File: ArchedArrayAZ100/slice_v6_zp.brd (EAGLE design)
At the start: 196.4 x 249.7 mm, 118 parts

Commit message: ArchedArray before moving board 6
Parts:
- removed F1: (no value), ZacksLib2:LITTLEFUSE_111_501
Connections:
- removed net N$284: F1.P2_1, F1.P2_2, U$1.P$2
- net N$1: now also D10.3; no longer D10.1
- net N$100: now also D43.3; no longer D43.1
- net N$101: now also D43.1; no longer D43.3
- net N$103: now also D44.3; no longer D44.1
- net N$104: now also D44.1; no longer D44.3
- net N$106: now also D40.3; no longer D40.1
- net N$107: now also D40.1; no longer D40.3
- net N$109: now also D35.3; no longer D35.1
- net N$11: now also D12.3; no longer D12.1
- net N$110: now also D35.1; no longer D35.3
- net N$113: now also D48.1; no longer D48.3
- net N$114: now also D48.3; no longer D48.1
- net N$115: now also D47.3; no longer D47.1
- net N$116: now also D47.1; no longer D47.3
- net N$119: now also D37.3; no longer D37.1
- net N$12: now also D12.1; no longer D12.3
- net N$121: now also D38.1; no longer D38.3
- net N$122: now also D34.3; no longer D34.1
- net N$123: now also D36.1; no longer D36.3
- net N$124: now also D36.3; no longer D36.1
- net N$125: now also D37.1; no longer D37.3
- net N$126: now also D38.3; no longer D38.1
- net N$127: now also D34.1; no longer D34.3
- net N$130: now also D41.3; no longer D41.1
- net N$131: now also D41.1; no longer D41.3
- net N$133: now also D33.3; no longer D33.1
- net N$135: now also D45.3; no longer D45.1
- net N$136: now also D45.1; no longer D45.3
- net N$139: now also D46.3; no longer D46.1
- net N$14: now also D8.3; no longer D8.1
- net N$140: now also D33.1; no longer D33.3
- net N$141: now also D46.1; no longer D46.3
- net N$142: now also D58.3; no longer D58.1
- net N$144: now also D55.3; no longer D55.1
- net N$145: now also D55.1; no longer D55.3
- net N$147: now also D59.3; no longer D59.1
- net N$148: now also D59.1; no longer D59.3
- net N$15: now also D8.1; no longer D8.3
- net N$150: now also D60.3; no longer D60.1
- net N$151: now also D60.1; no longer D60.3
- net N$153: now also D56.3; no longer D56.1
- net N$154: now also D56.1; no longer D56.3
- net N$156: now also D51.3; no longer D51.1
- net N$157: now also D51.1; no longer D51.3
- net N$160: now also D64.1; no longer D64.3
- net N$161: now also D64.3; no longer D64.1
- net N$162: now also D63.3; no longer D63.1
- net N$163: now also D63.1; no longer D63.3
- net N$166: now also D53.3; no longer D53.1
- net N$168: now also D54.1; no longer D54.3
- net N$169: now also D50.3; no longer D50.1
- net N$17: now also D3.1; no longer D3.3
- net N$170: now also D52.1; no longer D52.3
- net N$171: now also D52.3; no longer D52.1
- net N$172: now also D53.1; no longer D53.3
- net N$173: now also D54.3; no longer D54.1
- net N$174: now also D50.1; no longer D50.3
- net N$177: now also D57.3; no longer D57.1
- net N$178: now also D57.1; no longer D57.3
- net N$180: now also D49.3; no longer D49.1
- net N$182: now also D61.3; no longer D61.1
- net N$183: now also D61.1; no longer D61.3
- net N$186: now also D62.3; no longer D62.1
- net N$187: now also D49.1; no longer D49.3
- net N$188: now also D62.1; no longer D62.3
- net N$189: now also D74.3; no longer D74.1
- net N$191: now also D71.3; no longer D71.1
- net N$192: now also D71.1; no longer D71.3
- net N$194: now also D75.3; no longer D75.1
- net N$195: now also D75.1; no longer D75.3
- net N$197: now also D76.3; no longer D76.1
- net N$198: now also D76.1; no longer D76.3
- net N$2: now also D3.3; no longer D3.1
- net N$20: now also D16.1; no longer D16.3
- net N$200: now also D72.3; no longer D72.1
- net N$201: now also D72.1; no longer D72.3
- net N$203: now also D67.3; no longer D67.1
- net N$204: now also D67.1; no longer D67.3
- net N$207: now also D80.1; no longer D80.3
- net N$208: now also D80.3; no longer D80.1
- net N$209: now also D79.3; no longer D79.1
- net N$21: now also D16.3; no longer D16.1
- net N$210: now also D79.1; no longer D79.3
- net N$213: now also D69.3; no longer D69.1
- net N$215: now also D70.1; no longer D70.3
- net N$216: now also D66.3; no longer D66.1
- net N$217: now also D68.1; no longer D68.3
- net N$218: now also D68.3; no longer D68.1
- net N$219: now also D69.1; no longer D69.3
- net N$22: now also D15.3; no longer D15.1
- net N$220: now also D70.3; no longer D70.1
- net N$221: now also D66.1; no longer D66.3
- net N$224: now also D73.3; no longer D73.1
- net N$225: now also D73.1; no longer D73.3
- net N$227: now also D65.3; no longer D65.1
- net N$229: now also D77.3; no longer D77.1
- net N$23: now also D15.1; no longer D15.3
- net N$230: now also D77.1; no longer D77.3
- net N$233: now also D78.3; no longer D78.1
- net N$234: now also D65.1; no longer D65.3
- net N$235: now also D78.1; no longer D78.3
- net N$236: now also D90.3; no longer D90.1
- net N$238: now also D87.3; no longer D87.1
- net N$239: now also D87.1; no longer D87.3
- net N$241: now also D91.3; no longer D91.1
- net N$242: now also D91.1; no longer D91.3
- net N$244: now also D92.3; no longer D92.1
- net N$245: now also D92.1; no longer D92.3
- net N$247: now also D88.3; no longer D88.1
- net N$248: now also D88.1; no longer D88.3
- net N$25: now also D9.1; no longer D9.3
- net N$250: now also D83.3; no longer D83.1
- net N$251: now also D83.1; no longer D83.3
- net N$254: now also D96.1; no longer D96.3
- net N$255: now also D96.3; no longer D96.1
- net N$256: now also D95.3; no longer D95.1
- net N$257: now also D95.1; no longer D95.3
- net N$26: now also D4.1; no longer D4.3
- net N$260: now also D85.3; no longer D85.1
- net N$262: now also D86.1; no longer D86.3
- net N$263: now also D82.3; no longer D82.1
- net N$264: now also D84.1; no longer D84.3
- net N$265: now also D84.3; no longer D84.1
- net N$266: now also D85.1; no longer D85.3
- net N$267: now also D86.3; no longer D86.1
- net N$268: now also D82.1; no longer D82.3
- net N$27: now also D4.3; no longer D4.1
- net N$271: now also D89.3; no longer D89.1
- net N$272: now also D89.1; no longer D89.3
- net N$274: now also D81.3; no longer D81.1
- net N$276: now also D93.3; no longer D93.1
- net N$277: now also D93.1; no longer D93.3
- net N$28: now also D5.1; no longer D5.3
- net N$280: now also D94.3; no longer D94.1
- net N$281: now also D81.1; no longer D81.3
- net N$282: now also D94.1; no longer D94.3
- net N$288: now also D90.1; no longer D90.3
- net N$289: now also D42.1; no longer D42.3
- net N$290: now also D26.1; no longer D26.3
- net N$293: now also D10.1; no longer D10.3
- net N$298: now also D74.1; no longer D74.3
- net N$300: now also D58.1; no longer D58.3
- net N$31: now also D5.3; no longer D5.1
- net N$33: now also D6.1; no longer D6.3
- net N$34: now also D1.3; no longer D1.1
- net N$35: now also D2.3; no longer D2.1
- net N$36: now also D14.1; no longer D14.3
- net N$38: now also D6.3; no longer D6.1
- net N$39: now also D13.3; no longer D13.1
- net N$4: now also D7.3; no longer D7.1
- net N$40: now also D13.1; no longer D13.3
- net N$42: now also D2.1; no longer D2.3
- net N$45: now also D26.3; no longer D26.1
- net N$47: now also D14.3; no longer D14.1
- net N$49: now also D1.1; no longer D1.3
- net N$5: now also D7.1; no longer D7.3
- net N$50: now also D23.3; no longer D23.1
- net N$51: now also D23.1; no longer D23.3
- net N$53: now also D27.3; no longer D27.1
- net N$54: now also D27.1; no longer D27.3
- net N$56: now also D28.3; no longer D28.1
- net N$57: now also D28.1; no longer D28.3
- net N$59: now also D24.3; no longer D24.1
- net N$60: now also D24.1; no longer D24.3
- net N$62: now also D19.3; no longer D19.1
- net N$63: now also D19.1; no longer D19.3
- net N$66: now also D32.1; no longer D32.3
- net N$67: now also D32.3; no longer D32.1
- net N$68: now also D31.3; no longer D31.1
- net N$69: now also D31.1; no longer D31.3
- net N$7: now also D11.3; no longer D11.1
- net N$72: now also D21.3; no longer D21.1
- net N$74: now also D22.1; no longer D22.3
- net N$75: now also D18.3; no longer D18.1
- net N$76: now also D20.1; no longer D20.3
- net N$77: now also D20.3; no longer D20.1
- net N$78: now also D21.1; no longer D21.3
- net N$79: now also D22.3; no longer D22.1
- net N$8: now also D9.3; no longer D9.1
- net N$80: now also D18.1; no longer D18.3
- net N$83: now also D25.3; no longer D25.1
- net N$84: now also D25.1; no longer D25.3
- net N$86: now also D17.3; no longer D17.1
- net N$88: now also D29.3; no longer D29.1
- net N$89: now also D29.1; no longer D29.3
- net N$9: now also D11.1; no longer D11.3
- net N$92: now also D30.3; no longer D30.1
- net N$93: now also D17.1; no longer D17.3
- net N$94: now also D30.1; no longer D30.3
- net N$95: now also D42.3; no longer D42.1
- net N$97: now also D39.3; no longer D39.1
- net N$98: now also D39.1; no longer D39.3
- net VCC: now also U$1.P$2; no longer F1.P1_1, F1.P1_2
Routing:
- net GSCLK: track 81.2 -> 357.9 mm, vias 2 -> 11
- net VCC: track 1271.0 -> 1304.7 mm, vias 24 -> 22
- net N$284: track 11.3 -> 0.00 mm
- net N$126: track 30.0 -> 24.7 mm
- net N$4: track 30.6 -> 26.2 mm, vias 3 -> 1
- net N$125: track 18.3 -> 14.4 mm
- net N$22: track 32.1 -> 28.4 mm
- net N$2: track 31.1 -> 27.6 mm
- net N$110: track 28.4 -> 25.1 mm
- net N$20: track 52.2 -> 48.9 mm
- net N$139: track 23.0 -> 19.8 mm
- net N$293: track 56.3 -> 53.2 mm
- net N$114: track 24.0 -> 21.0 mm
- net N$141: track 21.1 -> 18.1 mm
- net N$100: track 24.7 -> 21.8 mm
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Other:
- board text removed: "7A Fuse"

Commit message: finished wiring Arched Array
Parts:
- moved U$1 34.0 mm to (98.0, 249.0), turned to 0 degrees
- moved D2 19.8 mm to (110.5, 208.0)
- moved D12 19.3 mm to (96.5, 208.0), turned to 90 degrees
- moved D8 19.2 mm to (82.5, 221.0), turned to 270 degrees
- moved CHIP_6 19.2 mm to (96.5, 218.5)
- moved D1 19.2 mm to (108.0, 216.0)
- moved D14 19.2 mm to (113.5, 216.0)
- moved D4 19.2 mm to (101.5, 208.0)
- moved D5 19.2 mm to (113.5, 224.0)
- moved D6 19.2 mm to (108.5, 224.0)
- moved D16 17.7 mm to (87.5, 225.5), turned to 270 degrees
- moved D13 16.7 mm to (113.5, 210.5)
- moved D10 15.6 mm to (78.5, 220.0), turned to 270 degrees
- moved C1 14.9 mm to (99.3, 229.0), turned to 180 degrees
- moved D15 14.3 mm to (91.5, 207.5)
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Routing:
- net VCC: track 1304.7 -> 1187.4 mm, vias 22 -> 18
- net GND: track 618.6 -> 558.2 mm, vias 16 -> 14
- net N$15: track 56.8 -> 11.1 mm
- net N$14: track 56.0 -> 11.3 mm
- net N$16: track 56.4 -> 12.1 mm
- net N$20: track 48.9 -> 5.80 mm
- net N$285: track 182.7 -> 140.7 mm, vias 3 -> 2
- net N$21: track 48.1 -> 7.83 mm
- net N$19: track 48.4 -> 8.61 mm
- net N$3: track 52.7 -> 19.8 mm
- net N$1: track 52.4 -> 20.6 mm
- net N$293: track 53.2 -> 22.6 mm
- net N$30: track 29.6 -> 9.67 mm
- net N$5: track 32.3 -> 13.6 mm
- net N$18: track 30.8 -> 12.8 mm
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
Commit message: added changes to ArchedArray board according to email
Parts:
- removed CHIP_6: TLC5955V0, ZacksLib:56-HTSSOP
- added F1: (no value), ZacksLib2:LITTLEFUSE_111_501
- added PWR: 2PIN_2AKLDHCX-8-0202-A, ZacksLib:TE_A32471
- D1, D10, D11, D12, D13, D14, D15, D16, D17, D18, D19, D2, D20, D21, D22, D23, D24, D25, D26, D27, D28, D29, D3, D30, D31, D32, D33, D34, D35, D36, D37, D38, D39, D4, D40, D41, D42, D43, D44, D45, D46, D47, D48, D49, D5, D50, D51, D52, D53, D54, D55, D56, D57, D58, D59, D6, D60, D61, D62, D63, D64, D65, D66, D67, D68, D69, D7, D70, D71, D72, D73, D74, D75, D76, D77, D78, D79, D8, D80, D81, D82, D83, D84, D85, D86, D87, D88, D89, D9, D90, D91, D92, D93, D94, D95, D96: device WallerLabLib:LED-RGB-THRU -> SparkFun-LED:LED-RGB-THRU
- U$1: value 2PIN_PWR3-6-12MM -> TLC5955V0; device WallerLabLib:2PIN_HOLES_PWR -> ZacksLib:56-HTSSOP
- moved SOUT2 181.2 mm to (69.5, 228.0), turned to 180 degrees
- moved SOUT6 78.6 mm to (32.5, 163.8), turned to 0 degrees
- moved SOUT4 31.6 mm to (-11.7, 141.4), turned to 270 degrees
- moved SOUT3 25.6 mm to (-19.0, 100.2)
- moved SOUT1 23.5 mm to (-24.5, 52.0), turned to 0 degrees
- moved D2 19.8 mm to (105.0, 227.0)
- moved D12 19.3 mm to (93.0, 227.0), turned to 270 degrees
- moved D8 19.2 mm to (97.5, 209.0), turned to 0 degrees
- moved D1 19.2 mm to (105.5, 235.0)
- moved D14 19.2 mm to (111.0, 235.0)
- moved D4 19.2 mm to (99.0, 227.0)
- moved D5 19.2 mm to (111.0, 243.0)
- moved D6 19.2 mm to (106.0, 243.0)
- moved D16 17.7 mm to (81.0, 209.0), turned to 0 degrees
- moved D13 16.7 mm to (111.0, 227.0)
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- renumbered CHIP_1 to U$4, CHIP_2 to U$5, CHIP_3 to U$6, CHIP_4 to U$2, CHIP_5 to U$3
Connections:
- new net N$284: F1.P2_1, F1.P2_2, PWR.PWR
- net DATA_OUT: now also U$2.P28; no longer CHIP_6.P28
- net GND: now also C2.2, C3.2, C4.2, C6.2, PWR.GND, U$1.P29, U$1.P56; no longer C2.1, C3.1, C4.1, C6.1, CHIP_6.P29, CHIP_6.P56, U$1.P$1
- net GSCLK: now also U$1.P55, U$3.P2; no longer CHIP_6.P55, U$3.P55
- net LAT: now also U$1.P3; no longer CHIP_6.P3
- net N$1: now also U$1.P8; no longer CHIP_6.P8
- net N$10: now also U$1.P13; no longer CHIP_6.P13
- net N$11: now also U$1.P26; no longer CHIP_6.P26
- net N$12: now also U$1.P27; no longer CHIP_6.P27
- net N$13: now also U$1.P25; no longer CHIP_6.P25
- net N$14: now also U$1.P11; no longer CHIP_6.P11
- net N$15: now also U$1.P12; no longer CHIP_6.P12
- net N$16: now also U$1.P10; no longer CHIP_6.P10
- net N$17: now also U$1.P21; no longer CHIP_6.P21
- net N$18: now also U$1.P19; no longer CHIP_6.P19
- net N$19: now also U$1.P4; no longer CHIP_6.P4
- net N$2: now also U$1.P20; no longer CHIP_6.P20
- net N$20: now also U$1.P6; no longer CHIP_6.P6
- net N$21: now also U$1.P5; no longer CHIP_6.P5
- net N$22: now also U$1.P23; no longer CHIP_6.P23
- net N$23: now also U$1.P24; no longer CHIP_6.P24
- net N$24: now also U$1.P22; no longer CHIP_6.P22
- net N$25: now also U$1.P33; no longer CHIP_6.P33
- net N$26: now also U$1.P30; no longer CHIP_6.P30
- net N$27: now also U$1.P31; no longer CHIP_6.P31
- net N$28: now also U$1.P51; no longer CHIP_6.P51
- net N$283: now also U$5.P28, U$6.P1; no longer U$2.P1, U$6.P28
- net N$285: now also U$2.P1; no longer CHIP_6.P1
- net N$286: now also U$6.P28; no longer U$2.P28
- net N$287: now also U$1.P1; no longer U$5.P1
- net N$29: now also U$1.P53; no longer CHIP_6.P53
- net N$291: now also U$1.P28, U$5.P1; no longer U$5.P28, U$6.P1
- net N$293: now also U$1.P9; no longer CHIP_6.P9
- net N$3: now also U$1.P7; no longer CHIP_6.P7
- net N$30: now also U$1.P35; no longer CHIP_6.P35
- net N$31: now also U$1.P52; no longer CHIP_6.P52
- net N$32: now also U$1.P47; no longer CHIP_6.P47
- net N$33: now also U$1.P45; no longer CHIP_6.P45
- net N$34: now also U$1.P40; no longer CHIP_6.P40
- net N$35: now also U$1.P37; no longer CHIP_6.P37
- net N$36: now also U$1.P48; no longer CHIP_6.P48
- net N$37: now also U$1.P41; no longer CHIP_6.P41
- net N$38: now also U$1.P46; no longer CHIP_6.P46
- net N$39: now also U$1.P43; no longer CHIP_6.P43
- net N$4: now also U$1.P17; no longer CHIP_6.P17
- net N$40: now also U$1.P42; no longer CHIP_6.P42
- net N$41: now also U$1.P44; no longer CHIP_6.P44
- net N$42: now also U$1.P36; no longer CHIP_6.P36
- net N$43: now also U$1.P38; no longer CHIP_6.P38
- net N$44: now also U$1.P32; no longer CHIP_6.P32
- net N$46: now also U$1.P50; no longer CHIP_6.P50
- net N$47: now also U$1.P49; no longer CHIP_6.P49
- net N$49: now also U$1.P39; no longer CHIP_6.P39
- net N$5: now also U$1.P18; no longer CHIP_6.P18
- net N$6: now also U$1.P16; no longer CHIP_6.P16
- net N$7: now also U$1.P14; no longer CHIP_6.P14
- net N$8: now also U$1.P34; no longer CHIP_6.P34
- net N$9: now also U$1.P15; no longer CHIP_6.P15
- net SCLK: now also U$1.P2, U$3.P55; no longer CHIP_6.P2, U$3.P2
- net VCC: now also C2.1, C3.1, C4.1, C6.1, F1.P1_1, F1.P1_2, U$1.P54; no longer C2.2, C3.2, C4.2, C6.2, CHIP_6.P54, U$1.P$2
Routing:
- net N$287: track 73.1 -> 342.7 mm, vias 0 -> 6
- net N$291: track 80.9 -> 302.7 mm, vias 1 -> 10
- net N$286: track 73.5 -> 208.3 mm, vias 2 -> 4
- net GND: track 558.2 -> 653.1 mm, vias 14 -> 17
- net SCLK: track 408.8 -> 498.1 mm, vias 5 -> 22
- net VCC: track 1187.4 -> 1262.7 mm, vias 18 -> 24
- net DATA_OUT: track 262.1 -> 191.6 mm, vias 2 -> 18
- net N$15: track 11.1 -> 57.5 mm
- net N$14: track 11.3 -> 56.5 mm
- net N$16: track 12.1 -> 56.4 mm
- net N$20: track 5.80 -> 49.6 mm
- net N$285: track 140.7 -> 99.4 mm, vias 2 -> 3
- net N$21: track 7.83 -> 48.5 mm
- net N$19: track 8.61 -> 48.4 mm
- net LAT: track 445.1 -> 483.2 mm, vias 20 -> 21
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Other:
- board text added: "7A Fuse"
- board text removed: "6"

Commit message: redid schematic for ArchedArray and modified LED part
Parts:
- renumbered U$1 to CHIP2
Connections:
- new net N$294: D67.2, D76.2
- net GND: now also C2.1, C3.1, C4.1, C6.1; no longer C2.2, C3.2, C4.2, C6.2
- net GSCLK: now also U$3.P55; no longer U$3.P2
- net SCLK: now also U$3.P2; no longer U$3.P55
- net VCC: now also C2.2, C3.2, C4.2, C6.2; no longer C2.1, C3.1, C4.1, C6.1, D67.2, D76.2
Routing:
- net SCLK: track 498.1 -> 0.00 mm, vias 22 -> 0
- net GSCLK: track 351.1 -> 0.00 mm, vias 2 -> 0
- net DATA_OUT: track 191.6 -> 0.00 mm, vias 18 -> 0
- net LAT: track 483.2 -> 376.5 mm
- net GND: track 653.1 -> 602.2 mm
- net DATA_IN: track 19.1 -> 0.00 mm, vias 1 -> 0
- net VCC: track 1262.7 -> 1249.7 mm
- net N$283: track 64.2 -> 59.3 mm
- net N$286: track 208.3 -> 205.6 mm
- net N$285: track 99.4 -> 96.9 mm
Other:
- board text added: "6"

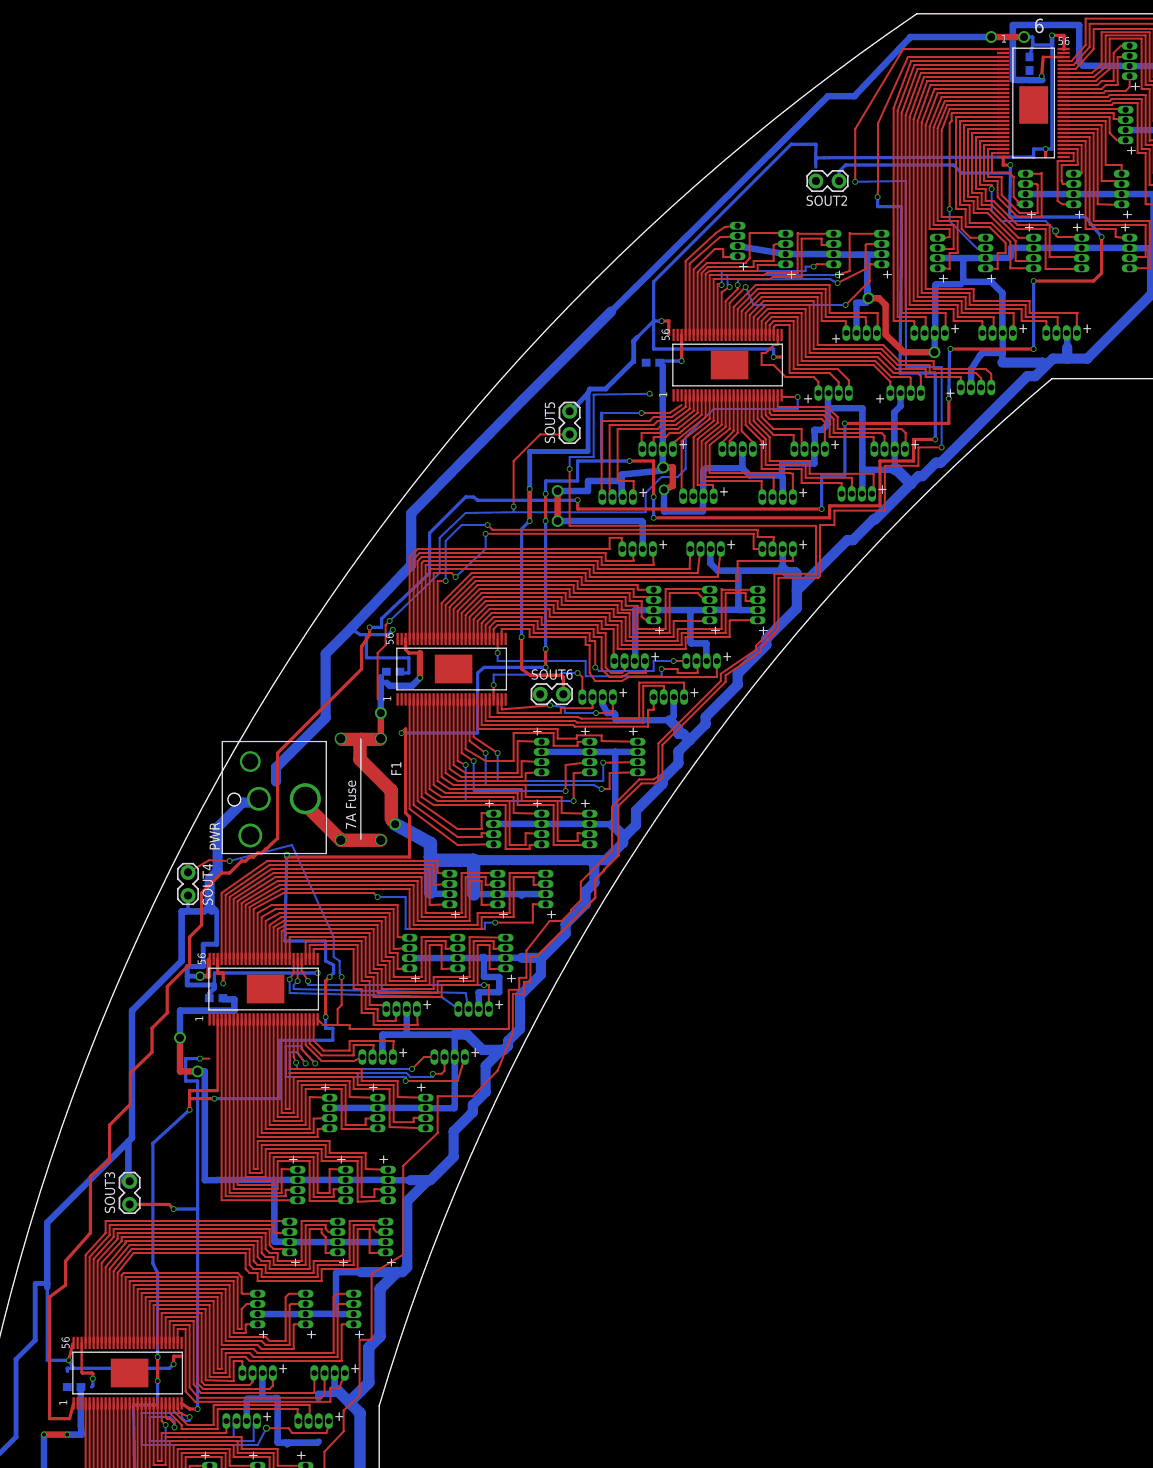
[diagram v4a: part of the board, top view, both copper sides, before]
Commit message: Finished TLC5955 initial board
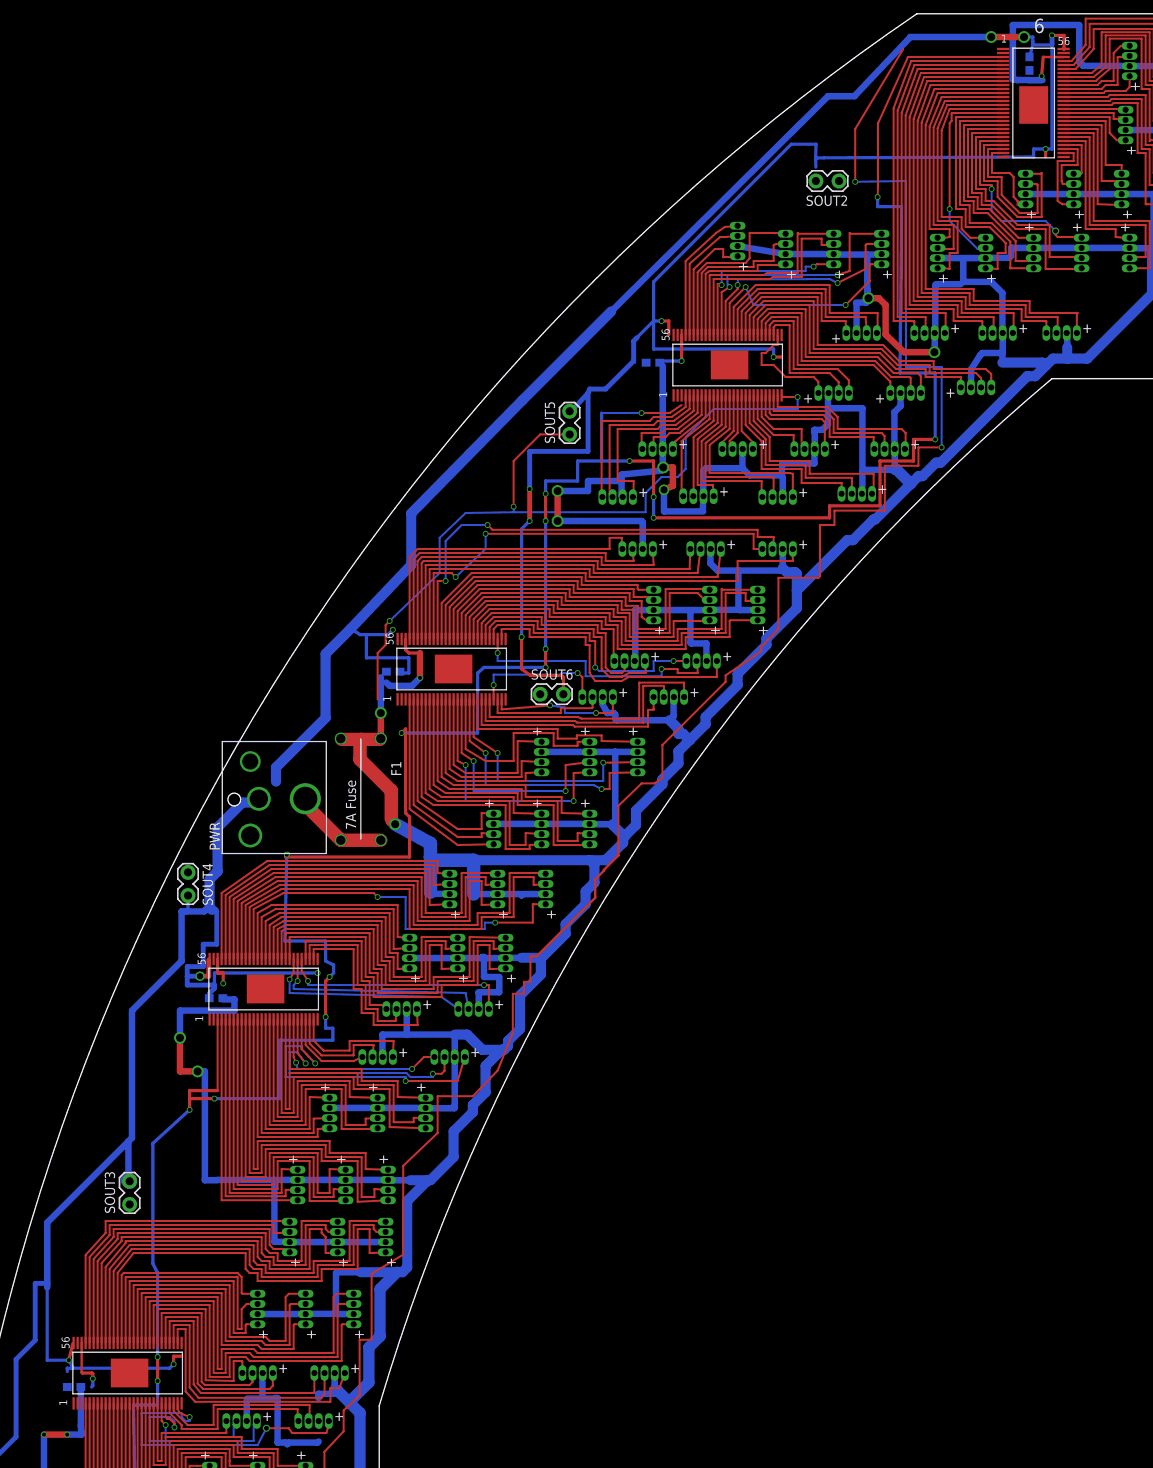
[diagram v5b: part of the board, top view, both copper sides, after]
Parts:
- renumbered CHIP2 to CHIP_6, U$2 to CHIP_4, U$3 to CHIP_5, U$4 to CHIP_1, U$5 to CHIP_2, U$6 to CHIP_3
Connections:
- removed net N$291 (its old number): CHIP_2.P1, CHIP_6.P28, SOUT2.1
- new net N$283: CHIP_3.P28, CHIP_4.P1, SOUT4.1
- net DATA_OUT: now also CHIP_6.P28, SOUT2.1; no longer CHIP_4.P28, SOUT6.1
- net N$285: now also CHIP_6.P1; no longer CHIP_4.P1
- net N$286: now also CHIP_4.P28, SOUT6.1; no longer CHIP_3.P28, SOUT4.1
- net N$287: now also CHIP_2.P1; no longer CHIP_6.P1
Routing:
- net N$291 (its old number): track 302.7 -> 0.00 mm, vias 10 -> 0
- net N$286: track 205.6 -> 0.00 mm, vias 4 -> 0
- net N$291: track 59.3 -> 0.00 mm, vias 3 -> 0
- net N$287: track 342.7 -> 330.2 mm
